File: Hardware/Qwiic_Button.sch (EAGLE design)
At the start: 31 parts, among them J2 QWIIC_RIGHT_ANGLE, J3 QWIIC_RIGHT_ANGLE, J7 ISP, U4 ATTINY84-ARDUINO

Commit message: post design review changes
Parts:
- LOGO3: value SFE_LOGO_NAME_FLAME.1_INCH -> SFE_LOGO_NAME.1_INCH; device SparkFun-Aesthetics:SFE_LOGO_NAME_FLAME.1_INCH -> SparkFun-Aesthetics:SFE_LOGO_NAME.1_INCH
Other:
- note added: "Fisher M."
- note removed: "Priyanka Makin"

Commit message: post checklist changes
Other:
- note added: "VIN: 1.8-5.5V"
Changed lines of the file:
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@@
 <text x="2.54" y="93.98" size="2.54" layer="97" font="vector">Address Jumpers</text>
 <text x="149.86" y="93.98" size="2.54" layer="97" font="vector">Button</text>
+<text x="2.54" y="177.8" size="1.27" layer="97" font="vector">VIN: 1.8-5.5V</text>
 </plain>
 <instances>

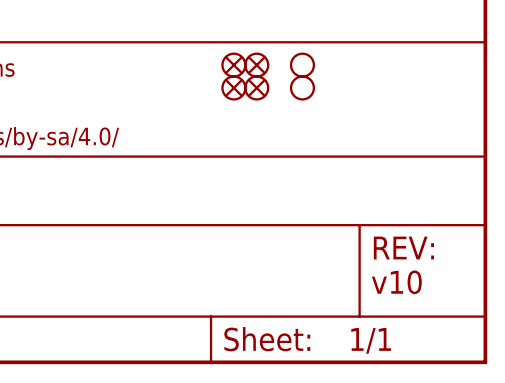
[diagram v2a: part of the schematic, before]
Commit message: adding polarity marker to button
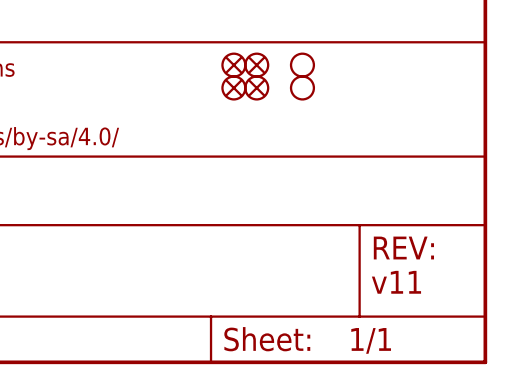
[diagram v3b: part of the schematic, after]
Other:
- note added: "v11"
- note removed: "v10"
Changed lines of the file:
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@@
 <?xml version="1.0" encoding="utf-8"?>
 <!DOCTYPE eagle SYSTEM "eagle.dtd">
-<eagle version="9.1.0">
+<eagle version="9.5.2">
 <drawing>
 <settings>
@@
 <sheet>
 <plain>
-<text x="236.22" y="7.62" size="2.54" layer="94" font="vector">v10</text>
+<text x="236.22" y="7.62" size="2.54" layer="94" font="vector">v11</text>
 <wire x1="147.32" y1="185.42" x2="147.32" y2="99.06" width="0.2032" layer="97" style="longdash"/>
 <wire x1="147.32" y1="99.06" x2="248.92" y2="99.06" width="0.2032" layer="97" style="longdash"/>
@@
 <attribute name="NAME" x="83.82" y="53.34" size="1.778" layer="95" font="vector" rot="R90"/>
 </instance>
-<instance part="LOGO2" gate="G$1" x="148.844" y="6.858"/>
-<instance part="LOGO3" gate="G$1" x="88.9" y="2.54"/>
-<instance part="LOGO4" gate="G$1" x="121.412" y="14.986"/>
+<instance part="LOGO2" gate="G$1" x="148.844" y="6.858" smashed="yes"/>
+<instance part="LOGO3" gate="G$1" x="88.9" y="2.54" smashed="yes"/>
+<instance part="LOGO4" gate="G$1" x="121.412" y="14.986" smashed="yes"/>
 </instances>
 <busses>
